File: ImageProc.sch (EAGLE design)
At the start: 117 parts, among them IC1 XC61GC3002HR-G, IC10 AT45DB642D-CNU, IC2 MIC5335-SPYMT, IC3 MIC5335-JGYMT, IC4 DSPIC33FJ128MC706A, IC5 AT86RF233-ZU, IC6 LTC6088, IC7 DRV8833RTY, IC8 DRV8833RTY, IC9 MPU-6000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

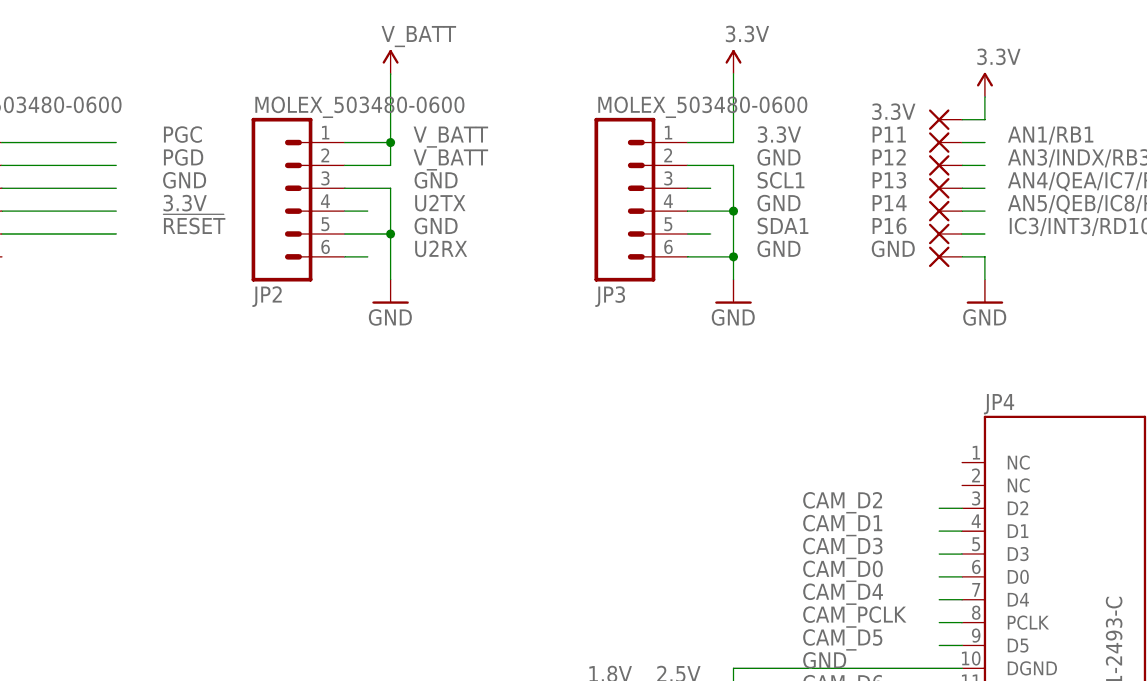
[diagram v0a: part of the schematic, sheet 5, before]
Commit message: Added Pads for PWM 1 and 2 to MOTOR_C_IN_2 and MOTOR_D_IN_2 on the top.
Added this both to the schematic and routed it on the board.
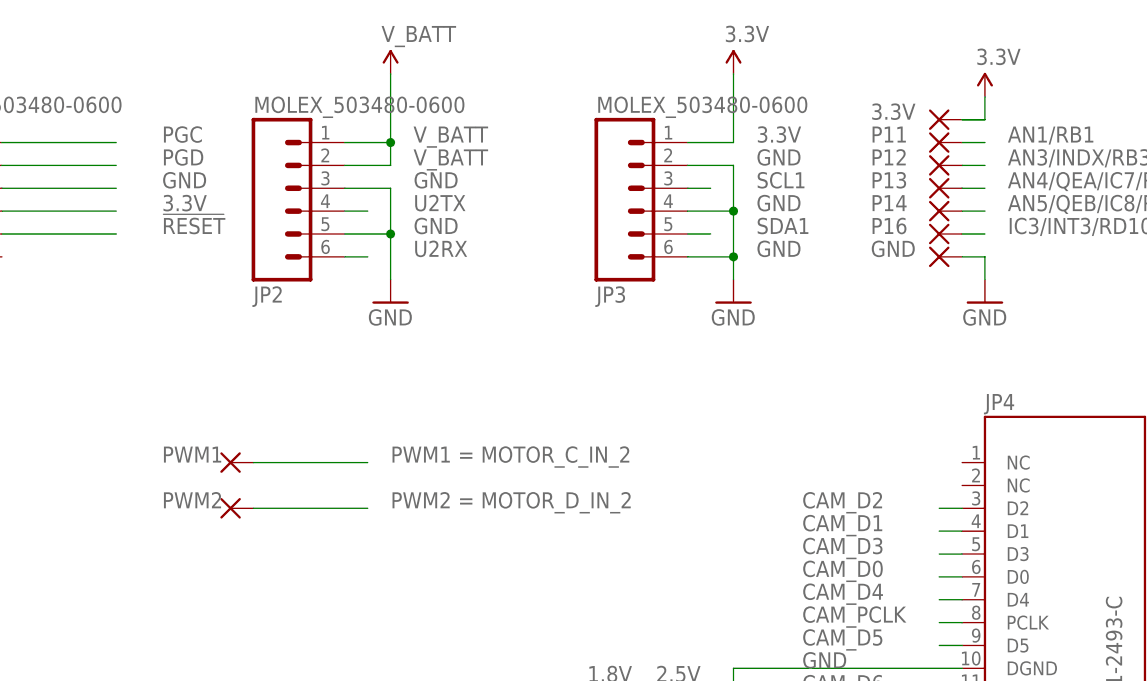
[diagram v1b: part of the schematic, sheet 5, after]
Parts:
- added PWM1, PWM2: EXT5, wirepad:SMD2
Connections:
- net MOTOR_C_IN2: now also PWM1.P
- net MOTOR_D_IN2: now also PWM2.P
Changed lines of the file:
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@@
 <part name="P+1" library="biomimetic" deviceset="3.3V" device=""/>
 <part name="GND24" library="biomimetic" deviceset="GND" device=""/>
+<part name="PWM1" library="wirepad" deviceset="SMD2" device="" value="EXT5">
+<attribute name="PWM1" value="MOTOR_C_IN_2"/>
+</part>
+<part name="PWM2" library="wirepad" deviceset="SMD2" device="" value="EXT5">
+<attribute name="PWM2" value="MOTOR_D_IN_2"/>
+</part>
 </parts>
 <sheets>
@@
 <instance part="P+1" gate="G$1" x="218.44" y="165.1"/>
 <instance part="GND24" gate="1" x="218.44" y="142.24"/>
+<instance part="PWM1" gate="1" x="134.62" y="124.46" smashed="yes">
+<attribute name="NAME" x="127" y="124.46" size="1.778" layer="95"/>
+<attribute name="PWM1" x="152.4" y="124.46" size="1.778" layer="96" display="both"/>
+</instance>
+<instance part="PWM2" gate="1" x="134.62" y="119.38" smashed="yes">
+<attribute name="NAME" x="127" y="119.38" size="1.778" layer="95"/>
+<attribute name="PWM2" x="152.4" y="119.38" size="1.778" layer="96" display="both"/>
+</instance>
 </instances>
 <busses>
@@
 <pinref part="P+1" gate="G$1" pin="3.3V"/>
 <wire x1="218.44" y1="162.56" x2="218.44" y2="165.1" width="0.1524" layer="91"/>
+<wire x1="215.9" y1="162.56" x2="218.44" y2="162.56" width="0.1524" layer="91"/>
 </segment>
 <segment>
@@
 </segment>
 </net>
+<net name="MOTOR_C_IN2" class="0">
+<segment>
+<pinref part="PWM1" gate="1" pin="P"/>
+<wire x1="137.16" y1="124.46" x2="149.86" y2="124.46" width="0.1524" layer="91"/>
+</segment>
+</net>
+<net name="MOTOR_D_IN2" class="0">
+<segment>
+<pinref part="PWM2" gate="1" pin="P"/>
+<wire x1="137.16" y1="119.38" x2="149.86" y2="119.38" width="0.1524" layer="91"/>
+</segment>
+</net>

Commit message: Fix transposed SDA1/SCL1 on dsPIC
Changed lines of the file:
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@@
 <layer number="93" name="Pins" color="2" fill="1" visible="yes" active="yes"/>
 <layer number="94" name="Symbols" color="4" fill="1" visible="yes" active="yes"/>
-<layer number="95" name="Names" color="7" fill="1" visible="no" active="yes"/>
+<layer number="95" name="Names" color="7" fill="1" visible="yes" active="yes"/>
 <layer number="96" name="Values" color="7" fill="1" visible="yes" active="yes"/>
 <layer number="97" name="Info" color="7" fill="1" visible="no" active="yes"/>
@@
 <attribute name="AUTHOR" value="Ryan Julian (ryanjulian@berkeley.edu)"/>
 <attribute name="DESIGN_NAME" value="ImageProc 2.5"/>
-<attribute name="REVISION" value="B"/>
+<attribute name="REVISION" value="C"/>
 <attribute name="YEAR" value="2012"/>
 </attributes>
